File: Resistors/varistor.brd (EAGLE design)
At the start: 114.3 x 30.2 mm, 2 parts

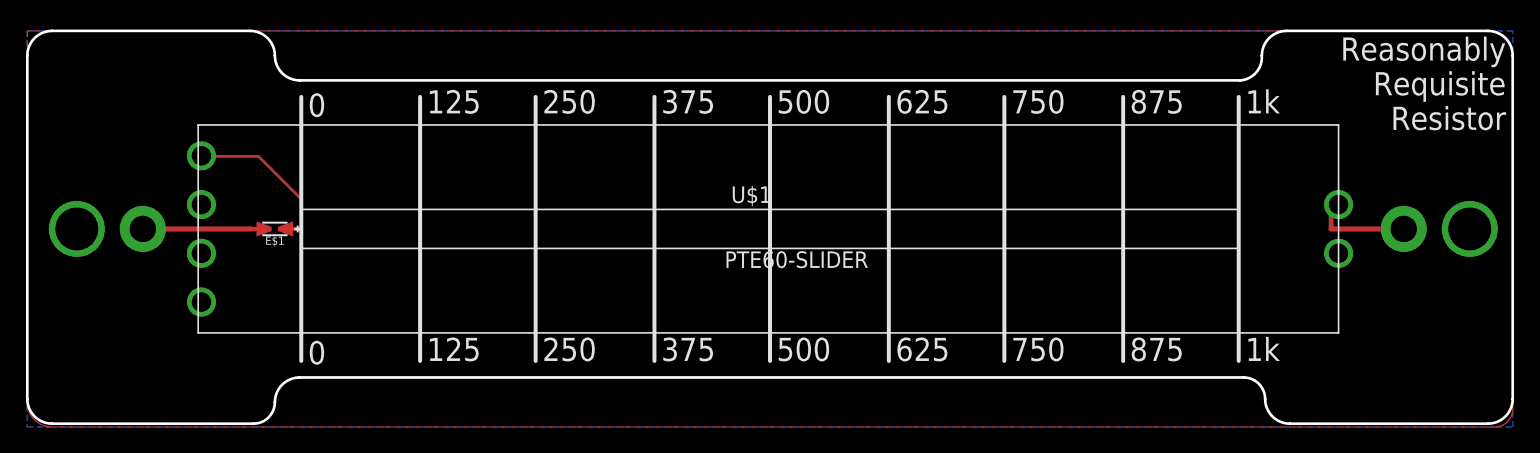
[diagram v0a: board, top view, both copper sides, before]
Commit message: Update part BOMs, correct minor varistor issue
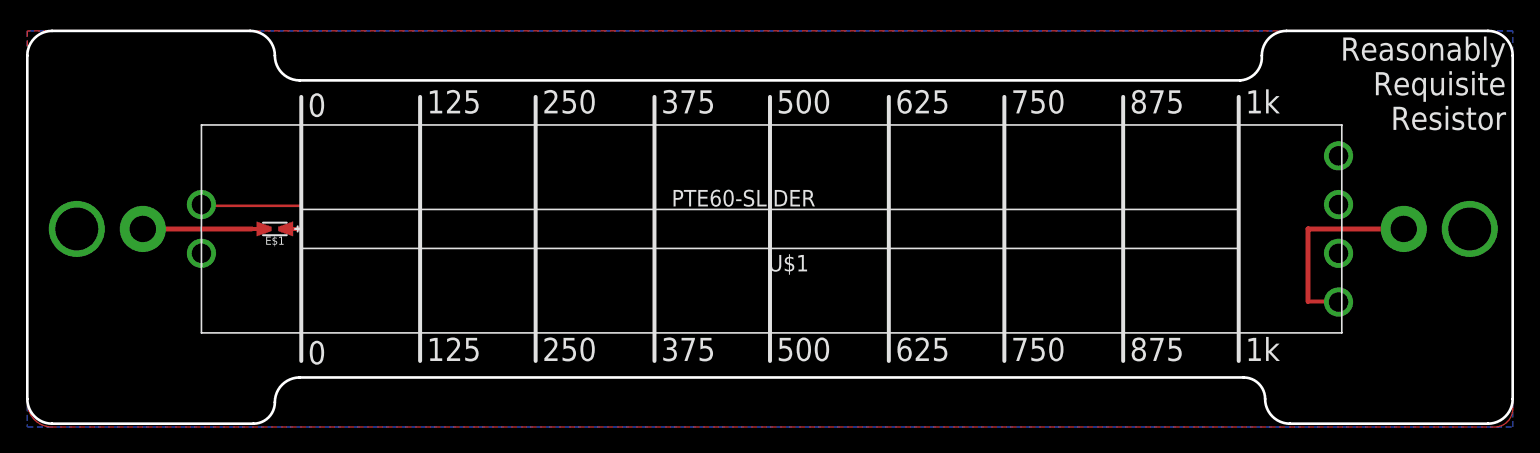
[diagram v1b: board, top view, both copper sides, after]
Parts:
- turned U$1 to 180 degrees
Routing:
- net S$4: track 7.87 -> 15.2 mm
- net S$3: track 21.7 -> 19.8 mm
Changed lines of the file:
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@@
 </autorouter>
 <elements>
-<element name="U$1" library="lt3092" package="SLIDER" value="PTE60-SLIDER" x="57.15" y="12.7"/>
+<element name="U$1" library="lt3092" package="SLIDER" value="PTE60-SLIDER" x="57.15" y="12.7" rot="R180"/>
 <element name="E$1" library="tekdemo" package="0402-0603-0805-UNIVERSAL" value="" x="19.05" y="12.7" rot="R180"/>
 </elements>
@@
 <via x="8.89" y="12.7" extent="1-16" drill="2.032" diameter="3.556"/>
 <wire x1="8.89" y1="12.7" x2="17.272" y2="12.7" width="0.381" layer="1"/>
-<wire x1="21.082" y1="12.7" x2="21.082" y2="14.986" width="0.2032" layer="1"/>
-<wire x1="21.082" y1="14.986" x2="17.78" y2="18.288" width="0.2032" layer="1"/>
-<wire x1="17.78" y1="18.288" x2="13.462" y2="18.288" width="0.2032" layer="1"/>
+<wire x1="21.082" y1="12.7" x2="21.082" y2="14.478" width="0.2032" layer="1"/>
+<wire x1="21.082" y1="14.478" x2="13.462" y2="14.478" width="0.2032" layer="1"/>
 <wire x1="17.272" y1="12.7" x2="18.034" y2="12.7" width="0.3048" layer="1"/>
 <wire x1="21.082" y1="12.7" x2="19.812" y2="12.7" width="0.3048" layer="1"/>
@@
 <signal name="S$4">
 <via x="105.918" y="12.7" extent="1-16" drill="2.032" diameter="3.556"/>
-<wire x1="105.918" y1="12.7" x2="100.33" y2="12.7" width="0.381" layer="1"/>
-<wire x1="100.33" y1="12.7" x2="100.33" y2="14.478" width="0.381" layer="1"/>
-<wire x1="100.33" y1="14.478" x2="100.838" y2="14.478" width="0.2032" layer="1"/>
+<wire x1="105.918" y1="12.7" x2="98.552" y2="12.7" width="0.381" layer="1"/>
+<wire x1="98.552" y1="12.7" x2="98.552" y2="7.112" width="0.381" layer="1"/>
+<wire x1="98.552" y1="7.112" x2="100.838" y2="7.112" width="0.3048" layer="1"/>
 </signal>
 <signal name="S$5">
